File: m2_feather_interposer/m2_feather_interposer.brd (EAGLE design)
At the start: 28.2 x 53.6 mm, 61 parts, among them J1 RICKK2_SPARK_M.2EKEY, U2 BQ24195, U3 MAX1704X, U6 XC9258A33EER-G, U7 XC8107SOT25

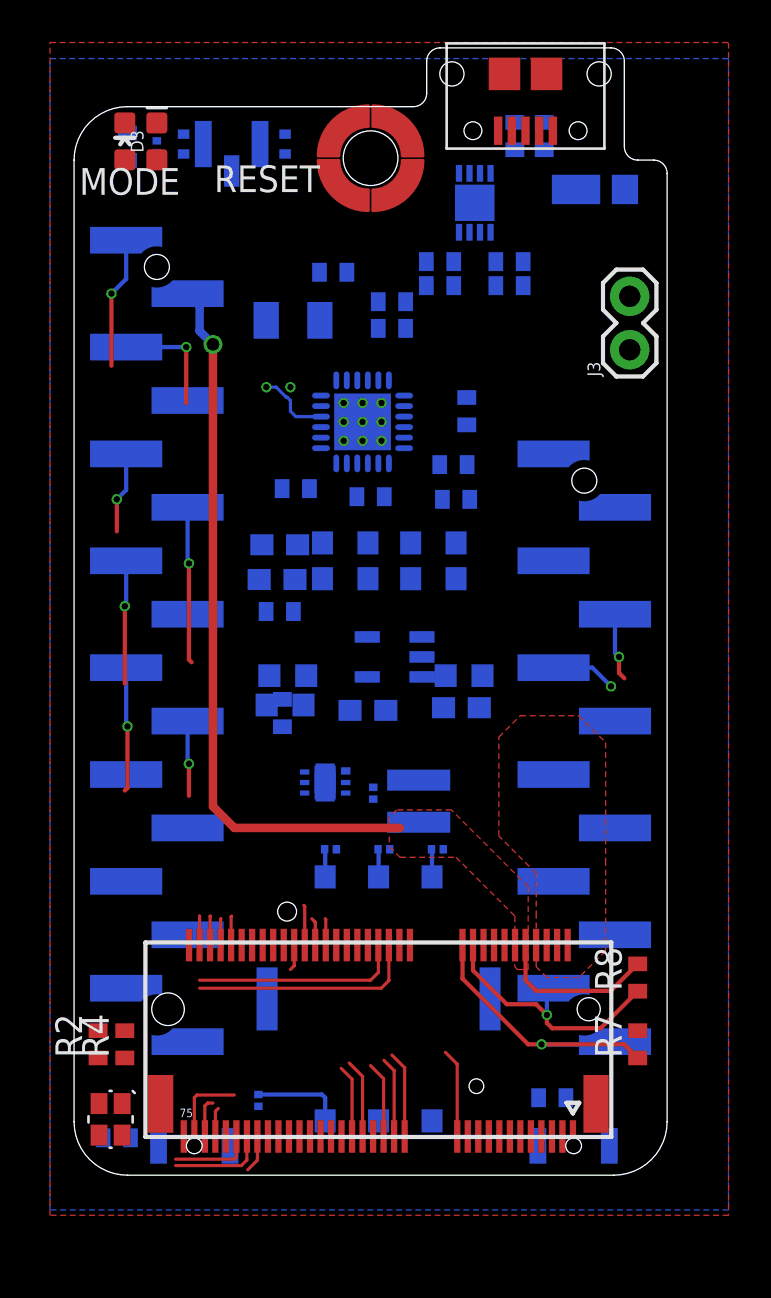
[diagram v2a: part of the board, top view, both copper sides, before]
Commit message: GPIO:draft layout done, LED: draft layout done, Buttons:draft layout done, SIM: draft layout done, NFC: draft layout done. Open items: fuel gauge, pmic, 3.3V reg
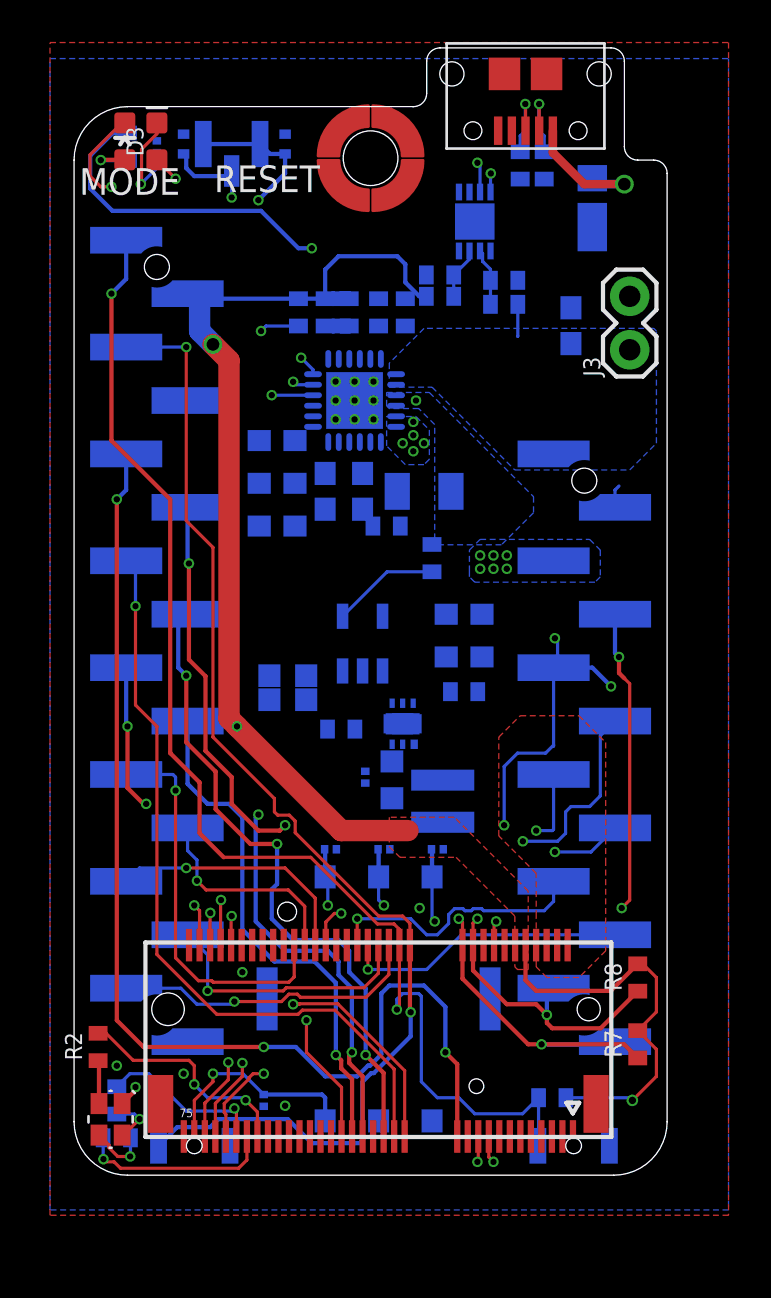
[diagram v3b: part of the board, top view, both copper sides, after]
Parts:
- moved C7 18.9 mm to (26.4, 43.6), turned to 90 degrees
- moved C12 12.3 mm to (17.7, 34.0), turned to 180 degrees
- moved C8 10.4 mm to (16.5, 35.7), turned to 270 degrees
- moved C6 10.3 mm to (12.4, 38.1), turned to 0 degrees
- moved C9 9.62 mm to (21.3, 27.8)
- moved C11 9.56 mm to (21.3, 26.2)
- moved C10 9.36 mm to (21.3, 29.8)
- moved R9 9.28 mm to (13.5, 44.2), turned to 90 degrees
- moved R10 9.03 mm to (14.7, 44.2), turned to 90 degrees
- moved R11_ 8.99 mm to (15.5, 44.2), turned to 270 degrees
- moved L1 8.92 mm to (18.2, 35.7), turned to 180 degrees
- moved R13_ 8.76 mm to (15.9, 44.2), turned to 270 degrees
- moved C20 8.46 mm to (13.0, 25.8)
- moved C5 6.56 mm to (12.4, 34.0), turned to 0 degrees
- moved C19 6.20 mm to (17.9, 22.0), turned to 90 degrees
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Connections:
- removed net N$4: R11.1, U$3.3
- removed net N$8: R13.1, U$3.2
- removed net USB-D+: U2.2
- removed net USB-D-: U2.3
- new net USBCON_N: R13.1, U$3.2, U2.3
- new net USBCON_P: R11.1, U$3.3, U2.2
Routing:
- net NFC1: track 0.00 -> 72.7 mm, vias 0 -> 2
- net NFC2: track 0.00 -> 71.4 mm, vias 0 -> 2
- net D7: track 4.48 -> 66.1 mm, vias 1 -> 5
- net SCL: track 12.5 -> 73.7 mm, vias 1 -> 4
- net SDA: track 15.0 -> 73.3 mm, vias 1 -> 4
- net /RESET: track 6.26 -> 60.2 mm, vias 1 -> 2
- net /MODE: track 5.52 -> 57.8 mm, vias 1 -> 2
- net A0: track 8.10 -> 54.1 mm, vias 1 -> 3
- net 3V3: track 41.4 -> 86.5 mm, vias 1 -> 4
- net BATINT: track 0.00 -> 42.0 mm, vias 0 -> 2
- net A3: track 3.62 -> 31.3 mm, vias 0 -> 3
- net A2: track 9.69 -> 36.2 mm
- net D6: track 1.38 -> 27.4 mm, vias 0 -> 2
- net D8: track 4.50 -> 30.4 mm, vias 1 -> 4
- net A1: track 11.6 -> 37.4 mm, vias 1 -> 3
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- added copper zone on layer 15, net 3V3
- added copper zone on layer 16, net BAT
- added copper zone on layer 16, net PMIC_VSYS
- added copper zone on layer 15, net VBUS
- added copper zone on layer 16, net VBUS
- removed copper zone on layer 2, net GND

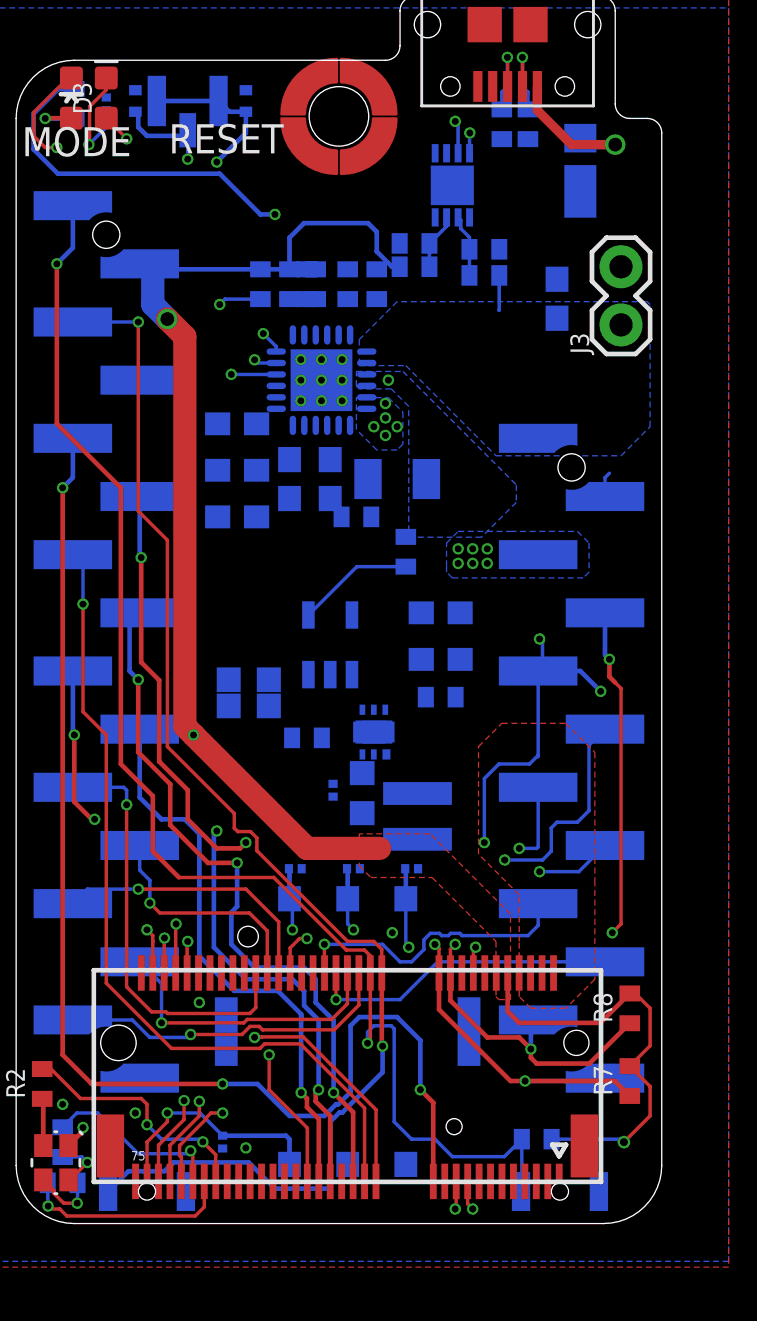
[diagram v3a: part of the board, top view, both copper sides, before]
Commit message: working through pmic, 3.3V and pwr switch layout:
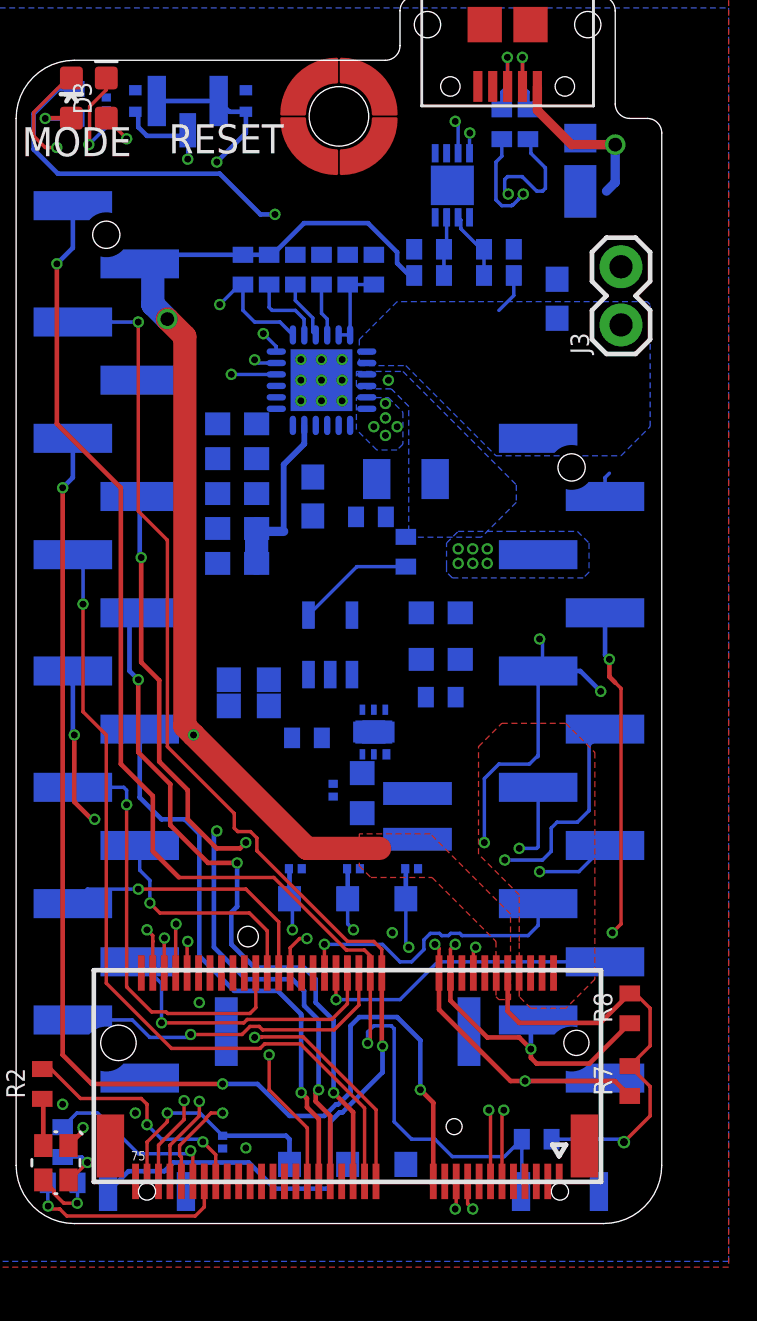
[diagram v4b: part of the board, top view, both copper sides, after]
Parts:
- added C13: 10uF, m2_feather_interposer:RICKK2_0603-CAP
- moved C4 3.14 mm to (12.4, 33.5), turned to 0 degrees
- moved R10 1.09 mm to (13.8, 44.8)
- moved C8 1.08 mm to (15.7, 34.9)
- moved C5 1.02 mm to (12.4, 35.1)
- moved R9 0.99 mm to (12.7, 44.8)
- moved R11_ 0.81 mm to (15.0, 44.8)
- moved R5 0.74 mm to (20.8, 44.6)
- moved R13_ 0.68 mm to (16.1, 44.8)
- moved C1 0.68 mm to (20.8, 45.7)
- moved R15 0.65 mm to (18.4, 44.8)
- moved R14 0.64 mm to (17.3, 44.8)
- moved C12 0.64 mm to (18.3, 34.0)
- moved C3 0.64 mm to (23.9, 45.7)
- moved R6 0.64 mm to (23.9, 44.6)
- moved C2 0.51 mm to (12.4, 36.6)
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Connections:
- net GND: now also C13.2
- net PMID: now also C13.1
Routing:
- net USB_D_N: track 0.00 -> 55.4 mm, vias 0 -> 2
- net USB_D_P: track 0.00 -> 54.4 mm, vias 0 -> 2
- net PMID: track 0.00 -> 7.76 mm
- net TS: track 0.00 -> 3.89 mm
- net OTG: track 0.00 -> 3.43 mm
- net BATINT: track 42.0 -> 45.2 mm
- net BQCE: track 0.00 -> 2.57 mm
- net ILIM: track 0.00 -> 2.30 mm
- net VUSB: track 7.87 -> 10.1 mm

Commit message: added draft bom
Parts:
- removed C13: 10uF, m2_feather_interposer:RICKK2_0603-CAP
- removed S5, S6: B3U-3000P-B, m2_feather_interposer:SW_B3U-3000P-B
- added S1, S2: B3U-3000P, m2_feather_interposer:SW_B3U-3000P
- D3: value P1.03 -> RED
- R19: value 1K -> 1k; device Particle:C0201_B -> adafruit:R0402
- moved U6 1.20 mm to (17.3, 25.0)
- moved R16 0.63 mm to (15.1, 23.9), turned to 90 degrees
- moved C8 0.51 mm to (15.7, 34.4)
- turned R19 to 90 degrees
- renumbered R13_ to R131
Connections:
- net /MODE: now also S1.2; no longer S5.2
- net /RESET: now also S2.2; no longer S6.2
- net GND: now also R19.2, S1.1, S2.1; no longer C13.2, R19.1, S5.1, S6.1
- net N$24: now also R19.1; no longer R19.2
- net PMID: no longer C13.1
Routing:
- net USBCON_P: track 3.65 -> 34.3 mm, vias 1 -> 2
- net USBCON_N: track 3.64 -> 33.6 mm, vias 1 -> 3
- net REGN: track 0.00 -> 16.6 mm, vias 0 -> 2
- net BATINT: track 45.2 -> 59.8 mm, vias 2 -> 3
- net BTST: track 0.00 -> 4.52 mm
- net PMID: track 7.76 -> 6.09 mm
- net N$24: track 5.04 -> 4.30 mm
